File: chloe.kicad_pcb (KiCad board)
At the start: 2 copper layers, 12.2 x 26.9 mm, 12 parts, among them IC1 ATTINY85-20SUR, P1 IO, P2 IO, P3 USB_A, U1 WS2812

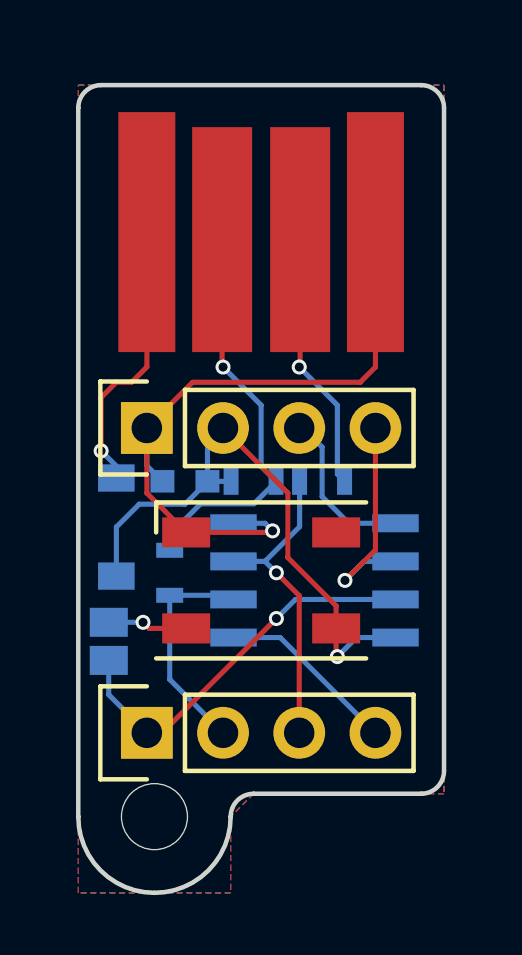
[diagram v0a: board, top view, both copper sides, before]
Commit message: Rotated 90deg
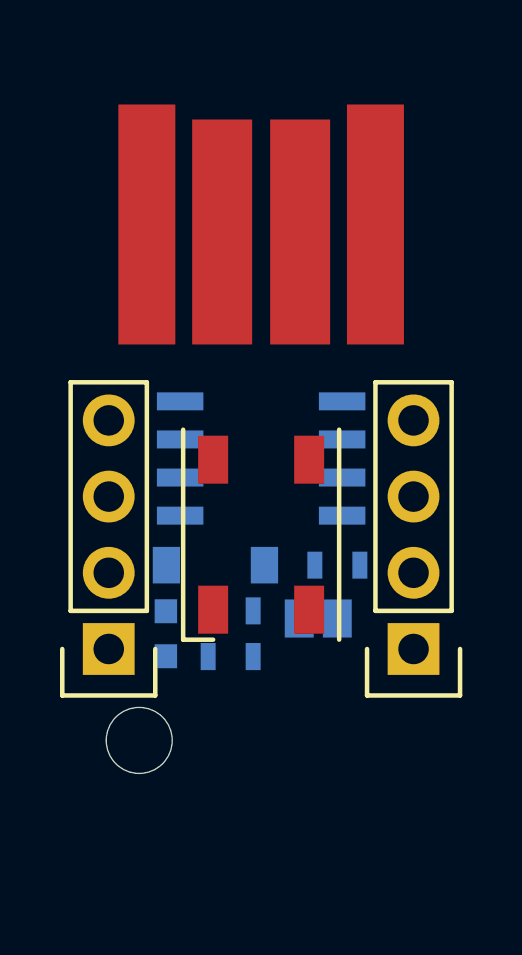
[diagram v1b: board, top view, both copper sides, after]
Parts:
- moved P2 9.32 mm to (166.4, 106.4), turned to 180 degrees
- moved P1 7.47 mm to (156.2, 106.4), turned to 180 degrees
- moved JP1 7.03 mm to (163.2, 105.4), turned to 90 degrees
- moved C1 5.12 mm to (158.1, 105.9), turned to 270 degrees
- moved IC1 4.44 mm to (161.3, 100.1), turned to 180 degrees
- moved R1 4.38 mm to (160.3, 105.2)
- moved D1 3.54 mm to (159.8, 103.6), turned to 0 degrees
- moved R2 3.45 mm to (160.3, 106.7), turned to 180 degrees
- moved R3 2.84 mm to (163.8, 103.6), turned to 180 degrees
- moved ? 2.59 mm to (157.2, 109.5), turned to 90 degrees
- moved U1 1.52 mm to (161.3, 102.6), turned to 270 degrees
- moved P3 0.25 mm to (161.3, 87.4)
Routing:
- net GND: track 23.3 -> 0.00 mm, vias 1 -> 0
- net +5V: track 19.5 -> 0.00 mm, vias 1 -> 0
- net Net-(P3-Pad2): track 13.6 -> 0.00 mm, vias 1 -> 0
- net Net-(IC1-Pad7): track 13.1 -> 0.00 mm, vias 1 -> 0
- net Net-(IC1-Pad3): track 10.4 -> 0.00 mm, vias 1 -> 0
- net Net-(D1-Pad2): track 9.34 -> 0.00 mm, vias 1 -> 0
- net Net-(P3-Pad3): track 8.70 -> 0.00 mm, vias 1 -> 0
- net Net-(IC1-Pad6): track 7.92 -> 0.00 mm, vias 1 -> 0
- net Net-(IC1-Pad2): track 7.50 -> 0.00 mm
- net Net-(IC1-Pad1): track 6.05 -> 0.00 mm
- net Net-(IC1-Pad5): track 5.49 -> 0.00 mm
- net Net-(JP1-Pad2): track 2.66 -> 0.00 mm, vias 1 -> 0
- removed copper zone on B.Cu, net GND
- removed copper zone on F.Cu, net GND
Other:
- board outline removed

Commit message: Routed connections
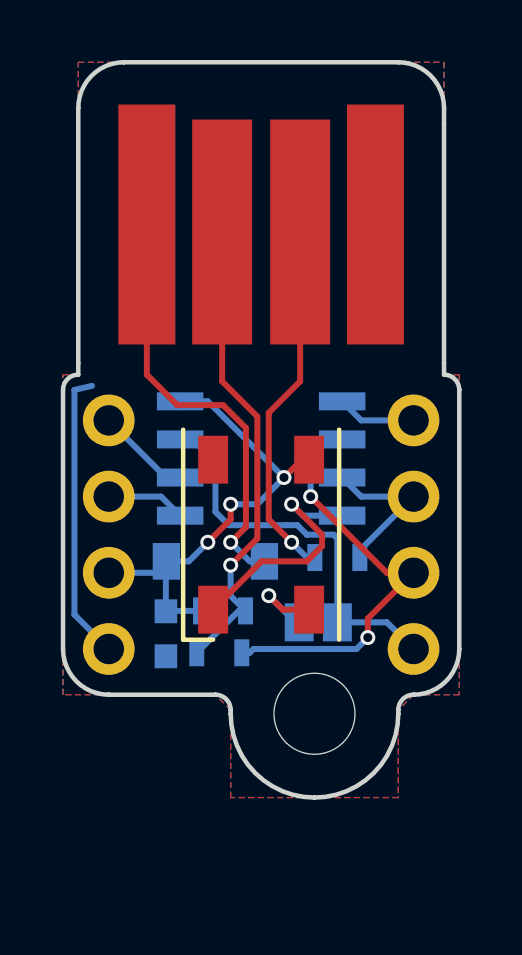
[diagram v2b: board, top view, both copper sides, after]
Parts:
- ?: footprint Mounting_Holes:MountingHole_2.2mm_M2 -> Mounting_Holes:MountingHole_2.7mm_M2.5
- P1, P2: moved to B.Cu
- moved ? 5.91 mm to (163.1, 108.6)
- moved R2 0.40 mm to (159.9, 106.6)
- moved R3 0.25 mm to (163.8, 103.4)
- moved R1 0.25 mm to (160.0, 105.2)
- moved D1 0.13 mm to (159.8, 103.5)
- moved JP1 0.13 mm to (163.2, 105.5)
- turned P1 to 0 degrees
- turned P2 to 0 degrees
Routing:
- net GND: track 0.00 -> 17.9 mm, vias 0 -> 1
- net +5V: track 0.00 -> 15.9 mm, vias 0 -> 3
- net Net-(P3-Pad2): track 0.00 -> 15.9 mm, vias 0 -> 1
- net Net-(D1-Pad2): track 0.00 -> 14.5 mm, vias 0 -> 1
- net Net-(IC1-Pad2): track 0.00 -> 14.3 mm, vias 0 -> 2
- net Net-(IC1-Pad7): track 0.00 -> 13.3 mm
- net Net-(P3-Pad3): track 0.00 -> 12.1 mm, vias 0 -> 1
- net Net-(IC1-Pad3): track 0.00 -> 5.17 mm
- net Net-(IC1-Pad6): track 0.00 -> 3.17 mm
- net Net-(JP1-Pad2): track 0.00 -> 2.92 mm, vias 0 -> 1
- net Net-(IC1-Pad5): track 0.00 -> 2.64 mm
- net Net-(IC1-Pad1): track 0.00 -> 2.64 mm
- added copper zone on B.Cu, net GND
- added copper zone on F.Cu, net GND
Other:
- board outline added: 13.2 x 24.5 mm
- net class Default: clearance 0.17 -> 0.1524; trace_width 0.17 -> 0.2
- rule trace_clearance: 0.17 -> 0.1524

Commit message: Cleanups and pinout
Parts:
- moved P3 0.13 mm to (161.3, 87.2)
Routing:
- net Net-(P3-Pad2): track 15.9 -> 18.3 mm
- net Net-(IC1-Pad2): track 14.3 -> 16.7 mm
- net Net-(JP1-Pad2): track 2.92 -> 0.56 mm
- net GND: track 17.9 -> 19.2 mm, vias 1 -> 2
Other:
- board text added: "5V"
- board text added: "GND"
- board text added: "P0"
- board text added: "P1"
- board text added: "P2"
- board text added: "P3"
- board text added: "P4"
- board text added: "P5"
